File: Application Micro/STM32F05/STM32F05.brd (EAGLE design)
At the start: 100 x 80 mm, 25 parts, among them Q1 ASF, T1 FDN340P

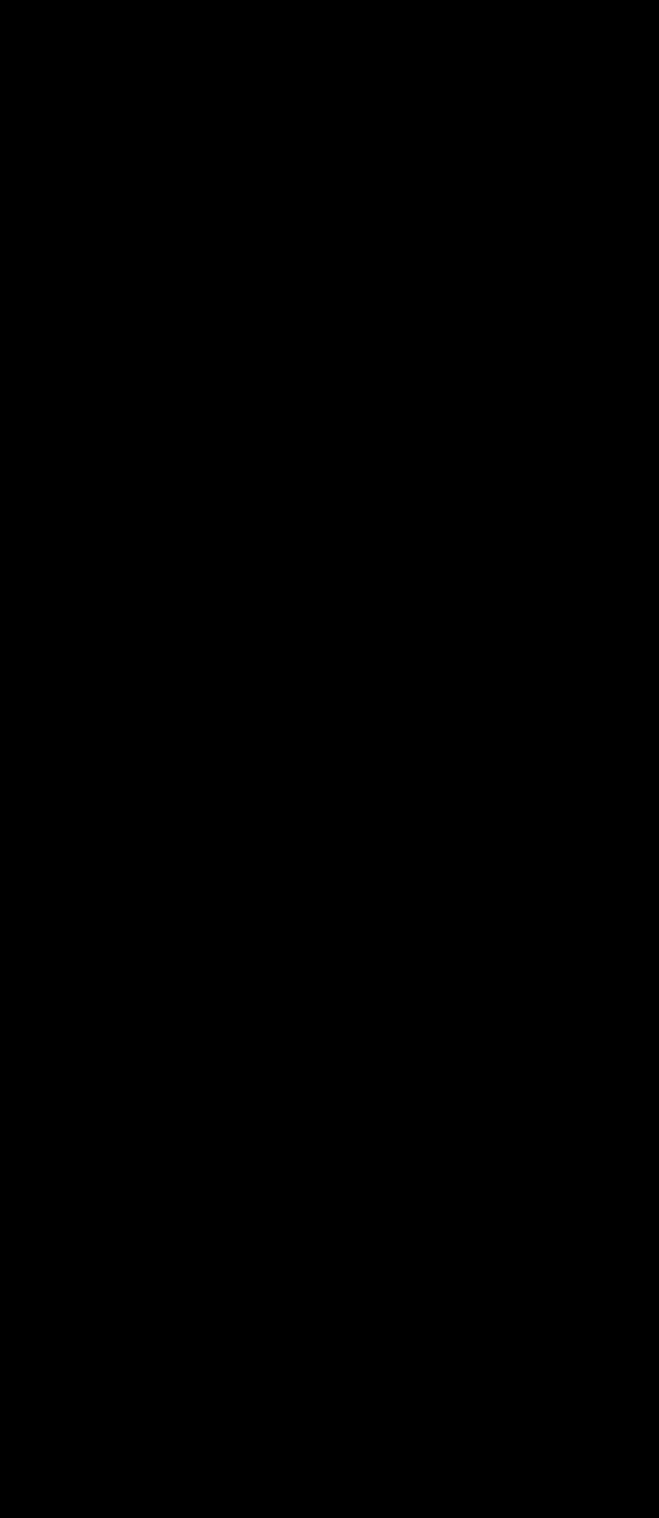
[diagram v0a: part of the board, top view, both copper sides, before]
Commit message: Updated application micro board
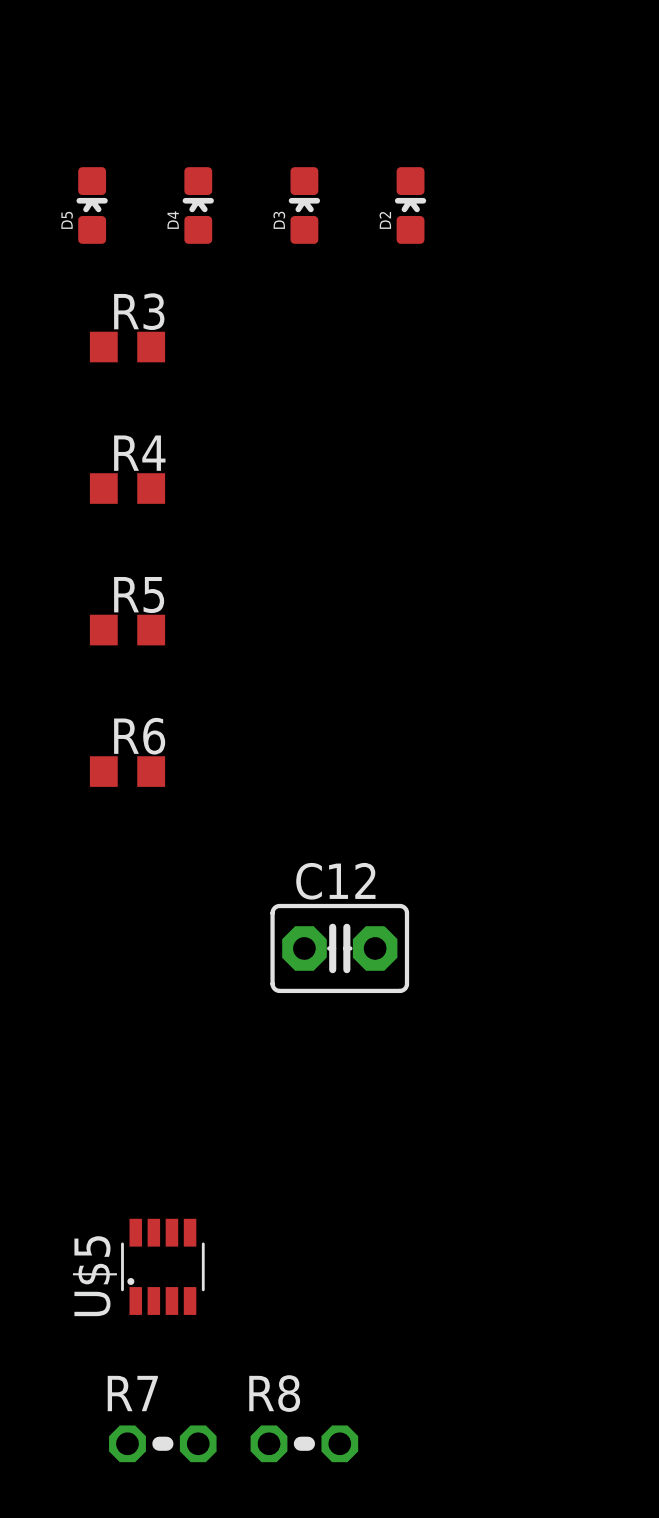
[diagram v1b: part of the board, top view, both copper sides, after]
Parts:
- added C12: 1 uF, capacitor-wima:C2.5-3
- added D2: Yellow, SparkFun-LED:LED-0603
- added D3: RED, SparkFun-LED:LED-0603
- added D4: BLUE, SparkFun-LED:LED-0603
- added D5: GREEN, SparkFun-LED:LED-0603
- added R3, R4, R5, R6: 10K, rcl:R0603
- added R7: 120, resistor:0204V
- added R8: 100k, resistor:0204V
- added U$5: MAX3051MAX3051, MAX3051 Library:SOT23-8L
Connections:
- new net +5V: D1.A, T1.3
- new net CANH: R7.1, U$5.7
- new net CANL: R7.2, U$5.6
- new net N$24: RN1.2, U$4.P3
- new net N$56: RN1.1, U$4.P2
- new net N$57: T1.1, U$4.P1
- new net N$58: D1.C, T1.2
- new net N$59: D2.A, R3.1
- new net N$60: D3.A, R4.1
- new net N$61: D4.A, R5.1
- new net N$62: D5.A, R6.1
- new net N$63: R8.1, U$5.8
- new net RXD: U$5.4
- new net TXD: U$5.1
- new net VCC: C12.2, U$5.3
- net GND: now also C12.1, D2.C, D3.C, D4.C, D5.C, R8.2, U$4.GND1, U$4.GND2, U$4.GND3, U$4.GND4, U$4.GND7, U$4.GND8, U$4.P4, U$4.P5, U$5.2
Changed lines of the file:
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@@
 <?xml version="1.0" encoding="utf-8"?>
 <!DOCTYPE eagle SYSTEM "eagle.dtd">
-<eagle version="7.1.0">
+<eagle version="7.3.0">
 <drawing>
 <settings>
@@
 <element name="U$3" library="DiscreteComponents" package="SW_2512" value="SWITCH" x="-19.05" y="40.64"/>
 <element name="U$4" library="Other" package="MICRO_B" value="MICROUSB" x="-38.1" y="38.1"/>
+<element name="D2" library="SparkFun-LED" package="LED-0603" value="Yellow" x="-59.69" y="2.54">
+<attribute name="PROD_ID" value="DIO-09003" x="-59.69" y="2.54" size="1.778" layer="27" display="off"/>
+</element>
+<element name="D3" library="SparkFun-LED" package="LED-0603" value="RED" x="-63.5" y="2.54">
+<attribute name="PROD_ID" value="DIO-00819" x="-63.5" y="2.54" size="1.778" layer="27" display="off"/>
+</element>
+<element name="D4" library="SparkFun-LED" package="LED-0603" value="BLUE" x="-67.31" y="2.54">
+<attribute name="PROD_ID" value="DIO-08575" x="-67.31" y="2.54" size="1.778" layer="27" display="off"/>
+</element>
+<element name="D5" library="SparkFun-LED" package="LED-0603" value="GREEN" x="-71.12" y="2.54">
+<attribute name="PROD_ID" value="DIO-00821" x="-71.12" y="2.54" size="1.778" layer="27" display="off"/>
+</element>
+<element name="R3" library="rcl" package="R0603" value="10K" x="-69.85" y="-2.54"/>
+<element name="R4" library="rcl" package="R0603" value="10K" x="-69.85" y="-7.62"/>
+<element name="R5" library="rcl" package="R0603" value="10K" x="-69.85" y="-12.7"/>
+<element name="R6" library="rcl" package="R0603" value="10K" x="-69.85" y="-17.78"/>
+<element name="U$5" library="MAX3051 Library" package="SOT23-8L" value="MAX3051MAX3051" x="-68.58" y="-35.56"/>
+<element name="C12" library="capacitor-wima" package="C2.5-3" value="1 uF" x="-62.23" y="-24.13"/>
+<element name="R7" library="resistor" package="0204V" value="120" x="-68.58" y="-41.91"/>
+<element name="R8" library="resistor" package="0204V" value="100k" x="-63.5" y="-41.91"/>
 </elements>
 <signals>
@@
 <contactref element="C11" pad="2"/>
 <contactref element="U$1" pad="28"/>
+<contactref element="U$4" pad="P5"/>
+<contactref element="U$4" pad="GND1"/>
+<contactref element="U$4" pad="GND2"/>
+<contactref element="U$4" pad="GND4"/>
+<contactref element="U$4" pad="GND3"/>
+<contactref element="U$4" pad="GND7"/>
+<contactref element="U$4" pad="GND8"/>
+<contactref element="U$4" pad="P4"/>
+<contactref element="D5" pad="C"/>
+<contactref element="D4" pad="C"/>
+<contactref element="D3" pad="C"/>
+<contactref element="D2" pad="C"/>
+<contactref element="U$5" pad="2"/>
+<contactref element="R8" pad="2"/>
+<contactref element="C12" pad="1"/>
+<wire x1="-62.23" y1="-41.91" x2="-68.905" y2="-36.785" width="0" layer="19" extent="1-1"/>
+<wire x1="-63.5" y1="-24.13" x2="-68.905" y2="-36.785" width="0" layer="19" extent="1-1"/>
+<wire x1="-63.5" y1="3.417" x2="-63.5" y2="-24.13" width="0" layer="19" extent="1-1"/>
+<wire x1="-67.31" y1="3.417" x2="-63.5" y2="3.417" width="0" layer="19" extent="1-1"/>
+<wire x1="-71.12" y1="3.417" x2="-67.31" y2="3.417" width="0" layer="19" extent="1-1"/>
+<wire x1="-59.69" y1="3.417" x2="-63.5" y2="3.417" width="0" layer="19" extent="1-1"/>
+<wire x1="-27.94" y1="5.87" x2="-59.69" y2="3.417" width="0" layer="19" extent="1-1"/>
+<wire x1="-24.84" y1="1.27" x2="-27.94" y2="5.87" width="0" layer="19" extent="1-1"/>
+<wire x1="-19.84" y1="1.27" x2="-24.84" y2="1.27" width="0" layer="19" extent="1-1"/>
+<wire x1="-24.84" y1="13.97" x2="-27.94" y2="5.87" width="0" layer="19" extent="1-1"/>
+<wire x1="-36.85" y1="29.33" x2="-24.84" y2="13.97" width="0" layer="19" extent="1-1"/>
+<wire x1="-37.1" y1="39.55" x2="-36.85" y2="29.33" width="0" layer="19" extent="1-1"/>
+<wire x1="-39.1" y1="39.55" x2="-37.1" y2="39.55" width="0" layer="19" extent="1-1"/>
+<wire x1="-34.5025" y1="39.55" x2="-37.1" y2="39.55" width="0" layer="19" extent="1-1"/>
+<wire x1="-41.6975" y1="39.55" x2="-39.1" y2="39.55" width="0" layer="19" extent="1-1"/>
+<wire x1="-36.8" y1="42.25" x2="-37.1" y2="39.55" width="0" layer="19" extent="1-1"/>
+<wire x1="-37.45" y1="42.25" x2="-36.8" y2="42.25" width="0" layer="19" extent="1-1"/>
+<wire x1="-35.6" y1="42.25" x2="-36.8" y2="42.25" width="0" layer="19" extent="1-1"/>
+<wire x1="-40.6" y1="42.25" x2="-41.6975" y2="39.55" width="0" layer="19" extent="1-1"/>
+<wire x1="-35.98" y1="46.99" x2="-35.6" y2="42.25" width="0" layer="19" extent="1-1"/>
+<wire x1="-42.33" y1="46.99" x2="-40.6" y2="42.25" width="0" layer="19" extent="1-1"/>
+<wire x1="-35.14" y1="52.07" x2="-35.98" y2="46.99" width="0" layer="19" extent="1-1"/>
+<wire x1="-29.63" y1="46.99" x2="-35.98" y2="46.99" width="0" layer="19" extent="1-1"/>
+<wire x1="-28.36" y1="52.07" x2="-29.63" y2="46.99" width="0" layer="19" extent="1-1"/>
+<wire x1="-23.28" y1="52.07" x2="-28.36" y2="52.07" width="0" layer="19" extent="1-1"/>
+<wire x1="-23.28" y1="46.99" x2="-23.28" y2="52.07" width="0" layer="19" extent="1-1"/>
+<wire x1="-16.93" y1="52.07" x2="-23.28" y2="52.07" width="0" layer="19" extent="1-1"/>
 <wire x1="-16.93" y1="46.99" x2="-16.93" y2="52.07" width="0" layer="19" extent="1-1"/>
-<wire x1="-23.28" y1="52.07" x2="-16.93" y2="52.07" width="0" layer="19" extent="1-1"/>
-<wire x1="-23.28" y1="46.99" x2="-23.28" y2="52.07" width="0" layer="19" extent="1-1"/>
-<wire x1="-28.36" y1="52.07" x2="-23.28" y2="52.07" width="0" layer="19" extent="1-1"/>
-<wire x1="-29.63" y1="46.99" x2="-28.36" y2="52.07" width="0" layer="19" extent="1-1"/>
-<wire x1="-35.98" y1="46.99" x2="-29.63" y2="46.99" width="0" layer="19" extent="1-1"/>
-<wire x1="-35.14" y1="52.07" x2="-35.98" y2="46.99" width="0" layer="19" extent="1-1"/>
-<wire x1="-42.33" y1="46.99" x2="-35.98" y2="46.99" width="0" layer="19" extent="1-1"/>
 <wire x1="-48.68" y1="46.99" x2="-42.33" y2="46.99" width="0" layer="19" extent="1-1"/>
 <wire x1="-55.03" y1="46.99" x2="-48.68" y2="46.99" width="0" layer="19" extent="1-1"/>
 <wire x1="-16.25" y1="40.64" x2="-16.93" y2="46.99" width="0" layer="19" extent="1-1"/>
 <wire x1="-53.76" y1="39.37" x2="-55.03" y2="46.99" width="0" layer="19" extent="1-1"/>
-<wire x1="-36.85" y1="29.33" x2="-35.98" y2="46.99" width="0" layer="19" extent="1-1"/>
-<wire x1="-24.84" y1="13.97" x2="-36.85" y2="29.33" width="0" layer="19" extent="1-1"/>
-<wire x1="-27.94" y1="5.87" x2="-24.84" y2="13.97" width="0" layer="19" extent="1-1"/>
-<wire x1="-24.84" y1="1.27" x2="-27.94" y2="5.87" width="0" layer="19" extent="1-1"/>
-<wire x1="-19.84" y1="1.27" x2="-24.84" y2="1.27" width="0" layer="19" extent="1-1"/>
 </signal>
 <signal name="N$3">
@@
 <contactref element="U$1" pad="6"/>
 </signal>
+<signal name="N$24">
+<contactref element="U$4" pad="P3"/>
+<contactref element="RN1" pad="2"/>
+<wire x1="-38.1" y1="42.25" x2="-44.05" y2="50.025" width="0" layer="19" extent="1-1"/>
+</signal>
+<signal name="N$56">
+<contactref element="U$4" pad="P2"/>
+<contactref element="RN1" pad="1"/>
+<wire x1="-38.75" y1="42.25" x2="-44.85" y2="50.025" width="0" layer="19" extent="1-1"/>
+</signal>
+<signal name="N$57">
+<contactref element="U$4" pad="P1"/>
+<contactref element="T1" pad="1"/>
+<wire x1="-39.4" y1="42.25" x2="-30.4546" y2="38.354" width="0" layer="19" extent="1-1"/>
+</signal>
+<signal name="+5V">
+<contactref element="T1" pad="3"/>
+<contactref element="D1" pad="A"/>
+<wire x1="-44.965" y1="39.37" x2="-29.4894" y2="40.386" width="0" layer="19" extent="1-1"/>
+</signal>
+<signal name="N$58">
+<contactref element="D1" pad="C"/>
+<contactref element="T1" pad="2"/>
+<wire x1="-31.4198" y1="40.386" x2="-49.015" y2="39.37" width="0" layer="19" extent="1-1"/>
+</signal>
+<signal name="N$59">
+<contactref element="D2" pad="A"/>
+<contactref element="R3" pad="1"/>
+<wire x1="-59.69" y1="1.663" x2="-70.7" y2="-2.54" width="0" layer="19" extent="1-1"/>
+</signal>
+<signal name="N$60">
+<contactref element="D3" pad="A"/>
+<contactref element="R4" pad="1"/>
+<wire x1="-63.5" y1="1.663" x2="-70.7" y2="-7.62" width="0" layer="19" extent="1-1"/>
+</signal>
+<signal name="N$61">
+<contactref element="D4" pad="A"/>
+<contactref element="R5" pad="1"/>
+<wire x1="-67.31" y1="1.663" x2="-70.7" y2="-12.7" width="0" layer="19" extent="1-1"/>
+</signal>
+<signal name="N$62">
+<contactref element="D5" pad="A"/>
+<contactref element="R6" pad="1"/>
+<wire x1="-71.12" y1="1.663" x2="-70.7" y2="-17.78" width="0" layer="19" extent="1-1"/>
+</signal>
+<signal name="N$63">
+<contactref element="U$5" pad="8"/>
+<contactref element="R8" pad="1"/>
+<wire x1="-69.555" y1="-34.335" x2="-64.77" y2="-41.91" width="0" layer="19" extent="1-1"/>
+</signal>
+<signal name="VCC">
+<contactref element="U$5" pad="3"/>
+<contactref element="C12" pad="2"/>
+<wire x1="-60.96" y1="-24.13" x2="-68.255" y2="-36.785" width="0" layer="19" extent="1-1"/>
+</signal>
+<signal name="CANL">
+<contactref element="U$5" pad="6"/>
+<contactref element="R7" pad="2"/>
+<wire x1="-68.255" y1="-34.335" x2="-67.31" y2="-41.91" width="0" layer="19" extent="1-1"/>
+</signal>
+<signal name="CANH">
+<contactref element="R7" pad="1"/>
+<contactref element="U$5" pad="7"/>
+<wire x1="-68.905" y1="-34.335" x2="-69.85" y2="-41.91" width="0" layer="19" extent="1-1"/>
+</signal>
+<signal name="TXD">
+<contactref element="U$5" pad="1"/>
+</signal>
+<signal name="RXD">
+<contactref element="U$5" pad="4"/>
+</signal>
 </signals>

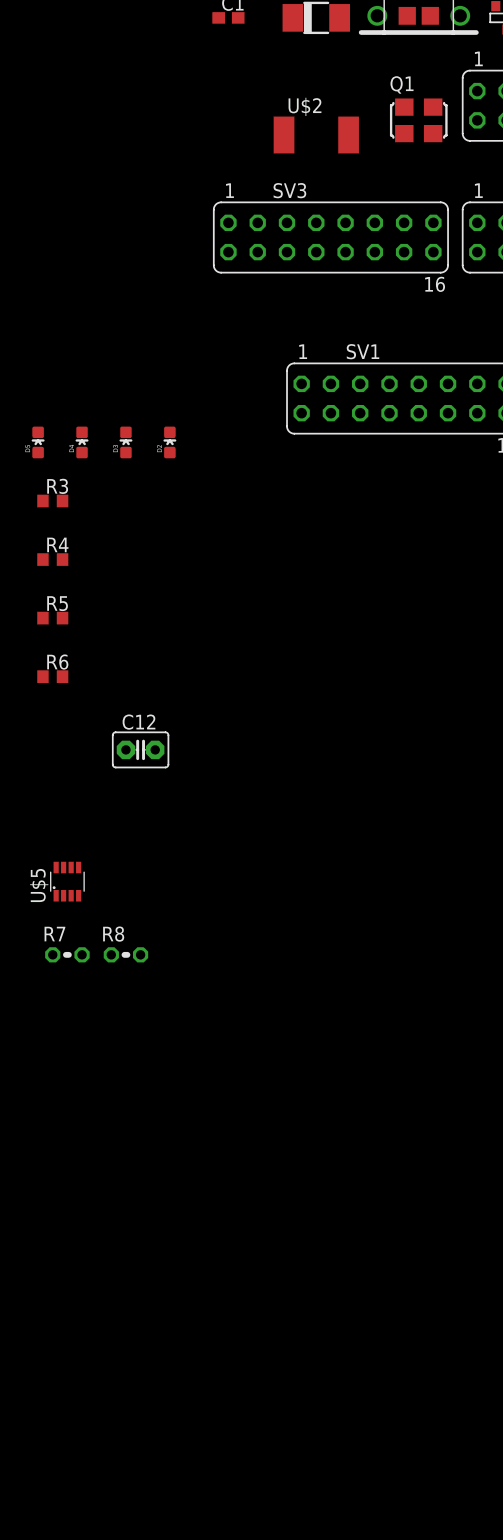
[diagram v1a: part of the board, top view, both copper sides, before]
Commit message: Continued work on application micro
Added circuitry for bi-directional linear regulator. Named some pins.
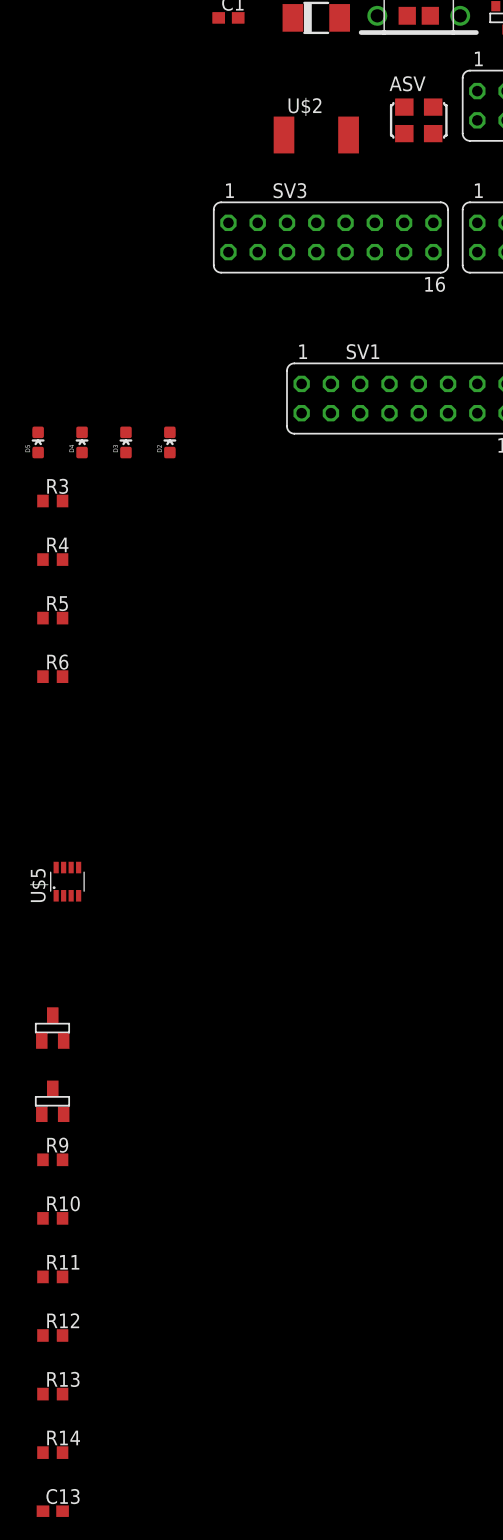
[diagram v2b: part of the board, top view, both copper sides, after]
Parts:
- removed C12: 1 uF, capacitor-wima:C2.5-3
- removed R7: 120, resistor:0204V
- removed R8: 100k, resistor:0204V
- added BSS138: n-chanel mosfet, DiscreteComponents:SOT-23-BSS138
- added C13: 0.1uF, rcl:C0603
- added R10, R11, R12, R9: 10K, rcl:R0603
- added R13: 120, rcl:R0603
- added R14: 100K, rcl:R0603
- added U$6: BSS138, DiscreteComponents:SOT-23-BSS138
- ASV: value ASF -> 8.000MHZ
- SV1: value (none) -> Left
- SV2: value (none) -> Top
- SV3: value (none) -> Bottom
- SV4: value (none) -> Right
- renumbered Q1 to ASV
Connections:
- removed net N$1: C1.1, U$1.31
- removed net N$10: U$1.16
- removed net N$11: U$1.17
- removed net N$12: U$1.20
- removed net N$13: U$1.21
- removed net N$14: U$1.22
- removed net N$15: U$1.23
- removed net N$16: U$1.41
- removed net N$17: U$1.42
- removed net N$18: U$1.43
- removed net N$19: U$1.44
- removed net N$2: C2.1, U$1.47
- removed net N$20: U$1.45
- removed net N$21: U$1.46
- removed net N$22: U$1.49
- removed net N$23: U$1.50
- removed net N$25: U$1.55
- removed net N$26: U$1.56
- removed net N$27: U$1.57
- removed net N$28: U$1.58
- removed net N$29: U$1.59
- removed net N$3: ASV.3, U$1.5
- removed net N$30: U$1.61
- removed net N$31: U$1.62
- removed net N$32: U$1.29
- removed net N$33: U$1.30
- removed net N$34: U$1.33
- removed net N$35: U$1.34
- removed net N$36: U$1.35
- removed net N$37: U$1.36
- removed net N$38: U$1.8
- removed net N$39: U$1.9
- removed net N$4: C11.1, R2.1, U$1.7, U$3.1
- removed net N$40: U$1.10
- removed net N$41: U$1.11
- removed net N$42: U$1.24
- removed net N$43: U$1.25
- removed net N$44: U$1.37
- removed net N$45: U$1.38
- removed net N$46: U$1.39
- removed net N$47: U$1.40
- removed net N$48: U$1.51
- removed net N$49: U$1.52
- removed net N$5: R1.2, U$1.60, U$2.1
- removed net N$50: U$1.53
- removed net N$51: U$1.2
- removed net N$52: U$1.3
- removed net N$53: U$1.4
- removed net N$54: U$1.54
- removed net N$55: U$1.6
- removed net N$6: U$1.14
- removed net N$7: U$1.15
- removed net N$8: U$1.26
- removed net N$9: U$1.27
- removed net VCC: C12.2, U$5.3
- new net BOOT0: R1.2, SV2.12, U$1.60, U$2.1
- new net NRST: C11.1, R2.1, SV1.7, U$1.7, U$3.1
- new net OSCIN: ASV.3, SV1.5, U$1.5
- new net OSCOUT: SV1.6, U$1.6
- new net PIN10: SV1.10, U$1.10
- new net PIN11: SV1.11, U$1.11
- new net PIN14: SV1.14, U$1.14
- new net PIN15: SV1.15, U$1.15
- new net PIN16: SV1.16, U$1.16
- new net PIN17: SV3.1, U$1.17
- new net PIN2: SV1.2, U$1.2
- new net PIN20: SV3.4, U$1.20
- new net PIN21: SV3.5, U$1.21
- new net PIN22: SV3.6, U$1.22
- new net PIN23: SV3.7, U$1.23
- new net PIN24: SV3.8, U$1.24
- new net PIN25: SV3.9, U$1.25
- new net PIN26: SV3.10, U$1.26
- new net PIN27: SV3.11, U$1.27
- new net PIN29: SV3.13, U$1.29
- new net PIN3: SV1.3, U$1.3
- new net PIN30: SV3.14, U$1.30
- new net PIN33: SV4.1, U$1.33
- new net PIN34: SV4.2, U$1.34
- new net PIN35: SV4.3, U$1.35
- new net PIN36: SV4.4, U$1.36
- new net PIN37: SV4.5, U$1.37
- new net PIN38: SV4.6, U$1.38
- new net PIN39: SV4.7, U$1.39
- new net PIN4: SV1.4, U$1.4
- new net PIN40: SV4.8, U$1.40
- new net PIN41: SV4.9, U$1.41
- new net PIN42: SV4.10, U$1.42
- new net PIN43: SV4.11, U$1.43
- new net PIN44: SV4.12, U$1.44
- new net PIN45: SV4.13, U$1.45
- new net PIN46: SV4.14, U$1.46
- new net PIN49: SV2.1, U$1.49
- new net PIN50: SV2.2, U$1.50
- new net PIN51: SV2.3, U$1.51
- new net PIN52: SV2.4, U$1.52
- new net PIN53: SV2.5, U$1.53
- new net PIN54: SV2.6, U$1.54
- new net PIN55: SV2.7, U$1.55
- new net PIN56: SV2.8, U$1.56
- new net PIN57: SV2.9, U$1.57
- new net PIN58: SV2.10, U$1.58
- new net PIN59: SV2.11, U$1.59
- new net PIN61: SV2.13, U$1.61
- new net PIN62: SV2.14, U$1.62
- new net PIN8: SV1.8, U$1.8
- new net PIN9: SV1.9, U$1.9
- new net SCL1: BSS138.3, R11.1
- new net SCL2: BSS138.2, R9.1
- new net SDA1: R12.1, U$6.3
- new net SDA2: R10.1, U$6.2
- new net VCAP_1: C1.1, SV3.15, U$1.31
- new net VCAP_2: C2.1, SV4.15, U$1.47
- net +3V3: now also BSS138.1, C13.1, R11.2, R12.2, SV1.1, SV1.13, SV2.16, SV3.16, SV3.3, SV4.16, U$5.3, U$6.1
- net +5V: now also R10.2, R9.2
- net CANH: now also R13.1; no longer R7.1
- net CANL: now also R13.2; no longer R7.2
- net GND: now also C13.2, R14.2, SV1.12, SV2.15, SV3.12, SV3.2; no longer C12.1, R8.2
- net N$63: now also R14.1; no longer R8.1
